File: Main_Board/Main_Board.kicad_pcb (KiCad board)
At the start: 4 copper layers, 35 parts, among them IC1 ZLDO1117K33TC, U1 STM32L152ZCTx

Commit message: Updated PCB
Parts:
- removed 56k (x2): R_2816_7142Metric_Pad3.20x4.45mm_HandSolder, Resistor_SMD:R_2816_7142Metric_Pad3.20x4.45mm_HandSolder
- removed 5Vin2: 5Vin, MountingHole:MountingHole_3mm_Pad
- removed CTimer (x2): CP_Elec_3x5.3, Capacitor_SMD:CP_Elec_3x5.3
- removed DIG0, DIG0_Matrix, DIG1, DIG1_Matrix, DIG2, DIG2_Matrix, DIG3, DIG3_Matrix, DIG4, DIG4_Matrix, DIG5, DIG5_Matrix, DIG6, DIG6_Matrix, DIG7, DIG7_Matrix: SolderWirePad_1x01_SMD_5x10mm, Connector_Wire:SolderWirePad_1x01_SMD_5x10mm
- removed GND: GND, MountingHole:MountingHole_3mm_Pad
- removed IC1: ZLDO1117K33TC, ZLDO1117K33TC-pcb-part-libraries:TO-252_1
- removed JTAGHeader1: Conn_ARM_JTAG_SWD_20, Connector_IDC:IDC-Header_2x06_P2.54mm_Horizontal
- removed Matrix_Cntrl1, TimerCntrl1: MAX6951CEE+, MAXIM:MAX6951CEE&plus_
- removed R4: R, Resistor_SMD:R_2816_7142Metric_Pad3.20x4.45mm_HandSolder
- removed REF** (x2): SolderWirePad_1x01_SMD_1x2mm, Connector_Wire:SolderWirePad_1x01_SMD_1x2mm
- removed Rx, Tx: MountingHole_Pad, MountingHole:MountingHole_3mm_Pad
- added 5V-3V3: ZLDO1117K33TC, TO-252_1, F.Cu at (166.2, 46.8)
- added 5V1: MountingHole_Pad, MountingHole:MountingHole_4.3mm_M4_Pad, F.Cu at (161.3, 30.5)
- added 7SEGDriver1: MAX6951CEE+, SOP64P602X173-17N, F.Cu at (111.3, 103.8)
- added BL1: MountingHole_Pad, MountingHole:MountingHole_4.3mm_M4_Pad_Via, F.Cu at (72.9, 116.7)
- added BR1: MountingHole_Pad, MountingHole:MountingHole_4.3mm_M4_Pad_Via, F.Cu at (191.7, 116.7)
- added C0: 100n, SamacSys_Parts:CAPC1005X55N, B.Cu at (111.8, 75.7)
- added C1: 100n, SamacSys_Parts:CAPC1005X55N, B.Cu at (115.8, 75.2)
- added C10: 100n, SamacSys_Parts:CAPC1005X55N, B.Cu at (111.8, 65.7)
- added C11: 100n, SamacSys_Parts:CAPC1005X55N, B.Cu at (111.7, 71.0)
- added C2: 100n, SamacSys_Parts:CAPC1005X55N, B.Cu at (121.5, 75.2)
- added C3: 100n, SamacSys_Parts:CAPC1005X55N, B.Cu at (128.0, 75.7)
- added C4: 100n, SamacSys_Parts:CAPC1005X55N, B.Cu at (127.1, 70.6)
- added C5: 100n, SamacSys_Parts:CAPC1005X55N, B.Cu at (127.0, 65.4)
- added C6: 100n, SamacSys_Parts:CAPC1005X55N, B.Cu at (127.5, 59.0)
- added C7: 100n, SamacSys_Parts:CAPC1005X55N, B.Cu at (120.5, 59.5)
- added C8: 100n, SamacSys_Parts:CAPC1005X55N, B.Cu at (115.2, 59.7)
- added C9: 100n, SamacSys_Parts:CAPC1005X55N, B.Cu at (111.6, 59.8)
- added CA0: 1u, SamacSys_Parts:CAPC1005X55N, B.Cu at (114.6, 62.5)
- added CA1: 10n, SamacSys_Parts:CAPC1005X55N, B.Cu at (114.6, 64.1)
- added CSET7SEG1: C_Small, Capacitor_SMD:C_1812_4532Metric_Pad1.57x3.40mm_HandSolder, F.Cu at (111.5, 109.1)
- added CSETLED1: C_Small, Capacitor_SMD:C_1812_4532Metric_Pad1.57x3.40mm_HandSolder, F.Cu at (81.5, 67.8)
- added Cbulk1: 4u7, SamacSys_Parts:CAPPRD200W52D500H1250, F.Cu at (176.0, 49.3)
- added Crst0: C, Capacitor_SMD:C_1812_4532Metric_Pad1.57x3.40mm_HandSolder, F.Cu at (175.8, 86.2)
- added GND1: MountingHole_Pad, MountingHole:MountingHole_4.3mm_M4_Pad, F.Cu at (172.2, 30.5)
- added HALLOUT1: MountingHole_Pad, MountingHole:MountingHole_2.7mm_Pad, F.Cu at (98.2, 29.2)
- added HALLSEL[0]1: MountingHole_Pad, MountingHole:MountingHole_2.7mm_Pad, F.Cu at (120.7, 29.2)
- added HALLSEL[1]1: MountingHole_Pad, MountingHole:MountingHole_2.7mm_Pad, F.Cu at (113.2, 29.2)
- added HALLSEL[2]1: MountingHole_Pad, MountingHole:MountingHole_2.7mm_Pad, F.Cu at (105.7, 29.2)
- added JTAGHEADER1: Conn_02x05_Odd_Even, Connector_PinHeader_2.00mm:PinHeader_2x05_P2.00mm_Vertical, F.Cu at (194.9, 64.1)
- added LA0: 39n, Inductor_SMD:L_01005_0402Metric_Pad0.57x0.30mm_HandSolder, B.Cu at (114.1, 66.0)
- added LEDDriver1: MAX6951CEE+, SOP64P602X173-17N, F.Cu at (87.9, 68.0)
- added R1: R_Small, Resistor_THT:R_Axial_DIN0309_L9.0mm_D3.2mm_P12.70mm_Horizontal, F.Cu at (152.7, 82.2)
- added R2: R, Resistor_THT:R_Axial_DIN0309_L9.0mm_D3.2mm_P12.70mm_Horizontal, F.Cu at (151.2, 39.9)
- added RSET7SEG1: R_Small, Resistor_THT:R_Axial_DIN0309_L9.0mm_D3.2mm_P12.70mm_Horizontal, F.Cu at (88.4, 105.9)
- added RSETLED1: R_Small, Resistor_THT:R_Axial_DIN0309_L9.0mm_D3.2mm_P12.70mm_Horizontal, F.Cu at (98.5, 67.6)
- added SEG0_7SEG1: MountingHole_Pad, MountingHole:MountingHole_2.5mm_Pad, F.Cu at (105.2, 117.9)
- added SEG0_LED1: MountingHole_Pad, MountingHole:MountingHole_2.5mm_Pad, F.Cu at (73.8, 64.6)
- added SEG1_7SEG1: MountingHole_Pad, MountingHole:MountingHole_2.5mm_Pad, F.Cu at (97.8, 117.9)
- added SEG1_LED1: MountingHole_Pad, MountingHole:MountingHole_2.5mm_Pad, F.Cu at (73.8, 56.9)
- added SEG2_7SEG1: MountingHole_Pad, MountingHole:MountingHole_2.5mm_Pad, F.Cu at (90.3, 117.9)
- added SEG2_LED1: MountingHole_Pad, MountingHole:MountingHole_2.5mm_Pad, F.Cu at (73.8, 49.2)
- added SEG3_7SEG1: MountingHole_Pad, MountingHole:MountingHole_2.5mm_Pad, F.Cu at (82.8, 117.9)
- added SEG3_LED1: MountingHole_Pad, MountingHole:MountingHole_2.5mm_Pad, F.Cu at (73.8, 41.4)
- added SEG4_7SEG1: MountingHole_Pad, MountingHole:MountingHole_2.5mm_Pad, F.Cu at (142.9, 117.9)
- added SEG4_LED1: MountingHole_Pad, MountingHole:MountingHole_2.5mm_Pad, F.Cu at (73.8, 103.3)
- added SEG5_7SEG1: MountingHole_Pad, MountingHole:MountingHole_2.5mm_Pad, F.Cu at (135.4, 117.9)
- added SEG5_LED1: MountingHole_Pad, MountingHole:MountingHole_2.5mm_Pad, F.Cu at (73.8, 95.5)
- added SEG6_7SEG1: MountingHole_Pad, MountingHole:MountingHole_2.5mm_Pad, F.Cu at (127.9, 117.9)
- added SEG6_LED1: MountingHole_Pad, MountingHole:MountingHole_2.5mm_Pad, F.Cu at (73.8, 87.8)
- added SEG7_7SEG1: MountingHole_Pad, MountingHole:MountingHole_2.5mm_Pad, F.Cu at (120.4, 117.9)
- added SEG7_LED1: MountingHole_Pad, MountingHole:MountingHole_2.5mm_Pad, F.Cu at (73.8, 80.1)
- added SEG8_7SEG1: MountingHole_Pad, MountingHole:MountingHole_2.5mm_Pad, F.Cu at (113.0, 117.9)
- added SEG8_LED1: MountingHole_Pad, MountingHole:MountingHole_2.5mm_Pad, F.Cu at (73.8, 72.4)
- added TL1: MountingHole_Pad, MountingHole:MountingHole_4.3mm_M4_Pad_Via, F.Cu at (73.1, 29.6)
- added TR1: MountingHole_Pad, MountingHole:MountingHole_4.3mm_M4_Pad_Via, F.Cu at (192.2, 29.5)
- added UART_Rx1: MountingHole_Pad, MountingHole:MountingHole_2.7mm_Pad, F.Cu at (161.9, 118.1)
- added UART_Tx1: MountingHole_Pad, MountingHole:MountingHole_2.7mm_Pad, F.Cu at (154.9, 118.1)
- added nRST1: SW_MEC_5G, Button_Switch_SMD:Panasonic_EVQPUL_EVQPUC, F.Cu at (157.6, 88.6)
- R3: footprint Resistor_SMD:R_2816_7142Metric_Pad3.20x4.45mm_HandSolder -> Resistor_THT:R_Axial_DIN0309_L9.0mm_D3.2mm_P12.70mm_Horizontal
- moved LED3V3 122.7 mm to (157.9, 47.2), turned to 0 degrees
- moved LED5V1 119.0 mm to (157.7, 40.6), turned to 0 degrees
- moved R3 116.5 mm to (144.5, 40.0), turned to 90 degrees
- moved U1 9.09 mm to (119.5, 67.4)
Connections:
- net /LED_Matrix_NSS renamed SPI3_NSS
- net /PH0OSC_IN renamed Net-(U1-Pad23)
- net /PH1OSC_OUT renamed Net-(U1-Pad24)
- net /PH2 renamed Net-(U1-Pad106)
- net /SPI1_MISO_AF5 renamed Net-(U1-Pad42)
- net /USART1_CK renamed Net-(U1-Pad100)
- net /USART1_CTS renamed Net-(U1-Pad103)
- net /USART1_RTS renamed Net-(U1-Pad104)
- net Net-(U1-Pad111) renamed SPI3_SCK
- net Net-(U1-Pad113) renamed SPI3_MOSI
- net Net-(U1-Pad134) renamed JTRST
- U1 pad 101: /USART1_TX_AF7 -> USART1_TX
- U1 pad 102: /USART1_RX_AF7 -> USART1_RX
- U1 pad 105: /JTMS-SWDIO -> JTMS-SWDIO
- U1 pad 107: +3V3 -> GND
- U1 pad 108: Net-(U1-Pad108) -> +3V3
- U1 pad 109: /JTCK-SWCLK -> JTCK-SWCLK
- U1 pad 110: /JTDI -> JTDI
- U1 pad 120: +3V3 -> GND
- U1 pad 121: Net-(U1-Pad121) -> +3V3
- U1 pad 130: +3V3 -> GND
- U1 pad 131: Net-(U1-Pad131) -> +3V3
- U1 pad 133: /JTDO -> JTDO-SWO
- U1 pad 143: +3V3 -> GND
- U1 pad 144: Net-(U1-Pad144) -> +3V3
- U1 pad 16: +3V3 -> GND
- U1 pad 17: Net-(U1-Pad17) -> +3V3
- U1 pad 25: Net-(U1-Pad25) -> +3V3
- U1 pad 30: Net-(U1-Pad30) -> GND
- U1 pad 33: Net-(U1-Pad33) -> +3.3VA
- U1 pad 34: /Hall_Select_[0] -> HALLSEL[0]
- U1 pad 35: /Hall_Select_[1] -> HALLSEL[1]
- U1 pad 36: /Hall_Select_[2] -> HALLSEL[2]
- U1 pad 37: /7Seg_NSS -> HALLOUT
- U1 pad 38: +3V3 -> GND
- U1 pad 39: Net-(U1-Pad39) -> +3V3
- U1 pad 41: /SPI1_SCK_AF5 -> DACOUT_2
- U1 pad 43: /SPI1_MOSI_AF5 -> SPI1_MOSI
- U1 pad 51: +3V3 -> GND
- U1 pad 52: Net-(U1-Pad52) -> +3V3
- U1 pad 61: +3V3 -> GND
- U1 pad 62: Net-(U1-Pad62) -> +3V3
- U1 pad 65: Net-(U1-Pad65) -> SPI1_NSS
- U1 pad 66: Net-(U1-Pad66) -> SPI1_SCK
- U1 pad 71: +3V3 -> GND
- U1 pad 72: Net-(U1-Pad72) -> +3V3
- U1 pad 73: Net-(U1-Pad73) -> SPI2_NSS
- U1 pad 74: Net-(U1-Pad74) -> SPI2_SCK
- U1 pad 76: Net-(U1-Pad76) -> SPI2_MOSI
- U1 pad 83: +3V3 -> GND
- U1 pad 84: Net-(U1-Pad84) -> +3V3
- U1 pad 94: +3V3 -> GND
- U1 pad 95: Net-(U1-Pad95) -> +3V3
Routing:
- net JTMS-SWDIO: track 0.00 -> 73.3 mm
- net JTDI: track 0.00 -> 71.8 mm, vias 0 -> 2
- net JTCK-SWCLK: track 0.00 -> 68.6 mm
- net JTDO-SWO: track 0.00 -> 64.4 mm
- net GND: track 58.0 -> 116.9 mm, vias 8 -> 30
- net USART1_RX: track 0.00 -> 58.0 mm
- net USART1_TX: track 0.00 -> 52.8 mm
- net /SEG4_LED: track 0.00 -> 41.3 mm
- net HALLOUT: track 0.00 -> 38.0 mm
- net /DIG_4_Matrix: track 36.8 -> 0.00 mm
- net /DIG_3_Matrix: track 36.4 -> 0.00 mm
- net /DIG_5_Matrix: track 35.9 -> 0.00 mm
- net /SEG4_7SEG: track 0.00 -> 35.1 mm
- net HALLSEL[0]: track 0.00 -> 32.7 mm
- net /SEG3_7SEG: track 0.00 -> 32.2 mm
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- added copper zone on In2.Cu, net +3V3
- added copper zone on In1.Cu, net GND
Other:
- net class 5V added: clearance 0.2, trace_width 1.27, via_dia 2.54, via_drill 1.524

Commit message: Updated Mainboard
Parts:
- removed 5V-3V3: ZLDO1117K33TC, TO-252_1
- removed C11: 100n, SamacSys_Parts:CAPC1005X55N
- removed Crst0: C, Capacitor_SMD:C_1812_4532Metric_Pad1.57x3.40mm_HandSolder
- removed HALLOUT1, HALLSEL[0]1, HALLSEL[1]1, HALLSEL[2]1, UART_Rx1, UART_Tx1: MountingHole_Pad, MountingHole:MountingHole_2.7mm_Pad
- removed R1: R_Small, Resistor_THT:R_Axial_DIN0309_L9.0mm_D3.2mm_P12.70mm_Horizontal
- removed SEG0_7SEG1, SEG0_LED1, SEG1_7SEG1, SEG1_LED1, SEG2_7SEG1, SEG2_LED1, SEG3_7SEG1, SEG3_LED1, SEG4_7SEG1, SEG4_LED1, SEG5_7SEG1, SEG5_LED1, SEG6_7SEG1, SEG6_LED1, SEG7_7SEG1, SEG7_LED1, SEG8_7SEG1, SEG8_LED1: MountingHole_Pad, MountingHole:MountingHole_2.5mm_Pad
- removed nRST1: SW_MEC_5G, Button_Switch_SMD:Panasonic_EVQPUL_EVQPUC
- added C12: 0.1u, SamacSys_Parts:CAPC2012X95N, F.Cu at (141.2, 43.5)
- added C13: 10u, SamacSys_Parts:CAPC2012X140N, F.Cu at (145.5, 40.3)
- added C14: 0.1u, SamacSys_Parts:CAPC2012X95N, F.Cu at (165.5, 45.2)
- added C15: 0.1u, SamacSys_Parts:CAPC2012X95N, F.Cu at (158.1, 47.5)
- added C16: 250u, Capacitor_THT:CP_Radial_D4.0mm_P2.00mm, F.Cu at (161.1, 38.5)
- added C18: 100n, SamacSys_Parts:CAPC2012X95N, F.Cu at (183.2, 46.5)
- added C19: 100n, SamacSys_Parts:CAPC2012X95N, F.Cu at (180.7, 46.6)
- added HallSensorHeader1: Conn_01x04_Male, Connector_PinHeader_2.54mm:PinHeader_1x04_P2.54mm_Vertical, F.Cu at (113.2, 26.6)
- added IC1: AZ1085CD-3.3TRG1, AZ1085CD33TRG1, F.Cu at (174.3, 49.6)
- added LED_Header1: Conn_01x09_Male, Connector_PinHeader_2.54mm:PinHeader_1x09_P2.54mm_Vertical, F.Cu at (70.6, 57.8)
- added LED_Header2: Conn_01x09_Male, Connector_PinHeader_2.54mm:PinHeader_1x09_P2.54mm_Vertical, F.Cu at (100.6, 119.4)
- added R4: 3300, Resistor_THT:R_Axial_DIN0309_L9.0mm_D3.2mm_P12.70mm_Horizontal, F.Cu at (126.9, 40.3)
- added R5: 150, Resistor_THT:R_Axial_DIN0309_L9.0mm_D3.2mm_P12.70mm_Horizontal, F.Cu at (126.8, 44.5)
- added R6: 100, Resistor_THT:R_Axial_DIN0309_L9.0mm_D3.2mm_P12.70mm_Horizontal, F.Cu at (142.1, 40.3)
- added R7: 10, Resistor_THT:R_Axial_DIN0309_L9.0mm_D3.2mm_P12.70mm_Horizontal, F.Cu at (158.0, 51.5)
- added SD_CARD1: 47352-1001, 47352-1001, F.Cu at (180.1, 73.5)
- added Speaker+1: MountingHole_Pad, MountingHole:MountingHole_2.5mm_Pad, F.Cu at (153.6, 28.4)
- added Speaker-1: MountingHole_Pad, MountingHole:MountingHole_2.5mm_Pad, F.Cu at (145.1, 28.2)
- added U2: LM386, SamacSys_Parts:SOP65P490X110-8N, F.Cu at (155.8, 43.8)
- added UARTHeader1: Conn_01x02_Male, Connector_PinHeader_2.54mm:PinHeader_1x02_P2.54mm_Vertical, F.Cu at (159.6, 119.5)
- C0, C1, C10, C2, C3, C4, C5, C6, C7, C8, C9: footprint SamacSys_Parts:CAPC1005X55N -> SamacSys_Parts:CAPC2012X95N
- CA0, LA0: moved to F.Cu
- CA1: footprint SamacSys_Parts:CAPC1005X55N -> SamacSys_Parts:CAPC2012X140N; moved to F.Cu
- CSET7SEG1, CSETLED1: value C_Small -> 47p; footprint Capacitor_SMD:C_1812_4532Metric_Pad1.57x3.40mm_HandSolder -> SamacSys_Parts:CAPC2012X75N
- RSET7SEG1, RSETLED1: value R_Small -> 47k; footprint Resistor_THT:R_Axial_DIN0309_L9.0mm_D3.2mm_P12.70mm_Horizontal -> SamacSys_Parts:RESC2012X60N
- moved LED5V1 109.2 mm to (237.3, 115.3), turned to 180 degrees
- moved R2 105.1 mm to (239.0, 97.8)
- moved R3 105.1 mm to (232.2, 97.9)
- moved LED3V3 100.3 mm to (237.1, 108.6), turned to 180 degrees
- moved JTAGHEADER1 31.8 mm to (194.3, 95.9)
- moved RSET7SEG1 20.1 mm to (108.4, 107.7), turned to 0 degrees
- moved RSETLED1 14.6 mm to (84.1, 65.1), turned to 270 degrees
- moved LA0 14.5 mm to (112.5, 51.5), turned to 180 degrees
- moved C8 11.9 mm to (111.7, 71.0), turned to 270 degrees
- moved CA1 11.4 mm to (113.2, 52.9)
- moved Cbulk1 11.1 mm to (186.6, 45.8)
- moved CA0 8.24 mm to (112.8, 54.5)
- moved 5V1 7.80 mm to (169.1, 30.5)
- moved GND1 7.66 mm to (179.8, 30.7), turned to 0 degrees
- moved CSETLED1 2.73 mm to (83.8, 69.2)
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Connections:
- U1 pad 112: Net-(U1-Pad112) -> SPI3_MISO
- U1 pad 114: Net-(U1-Pad114) -> SPI3_NSS
- U1 pad 25: +3V3 -> Net-(U1-Pad25)
- U1 pad 40: SPI3_NSS -> Net-(U1-Pad40)
- U1 pad 41: DACOUT_2 -> DAC_OUT
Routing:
- net GND: track 116.9 -> 179.7 mm, vias 30 -> 32
- net SPI3_MISO: track 0.00 -> 60.3 mm, vias 0 -> 2
- net SPI3_SCK: track 0.00 -> 60.0 mm, vias 0 -> 2
- net SPI3_MOSI: track 0.00 -> 57.8 mm, vias 0 -> 2
- net SPI3_NSS: track 0.00 -> 57.0 mm, vias 0 -> 2
- net +3V3: track 61.7 -> 97.6 mm, vias 27 -> 26
- net DAC_OUT: track 0.00 -> 28.0 mm, vias 0 -> 1
- net Net-(7SEGDriver1-Pad7): track 20.3 -> 3.26 mm, vias 1 -> 0
- net /SEG4_LED: track 41.3 -> 24.3 mm, vias 0 -> 1
- net +5V: track 14.9 -> 29.1 mm
- net Net-(LEDDriver1-Pad7): track 17.4 -> 3.45 mm, vias 1 -> 0
- net Net-(C16-Pad1): track 0.00 -> 13.5 mm
- net /SEG4_7SEG: track 35.1 -> 23.6 mm, vias 0 -> 1
- net Net-(C15-Pad1): track 0.00 -> 9.93 mm, vias 0 -> 1
- net Net-(C13-Pad1): track 0.00 -> 9.55 mm
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
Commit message: A
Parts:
- added C11: 30p, Capacitor_SMD:C_1206_3216Metric_Pad1.33x1.80mm_HandSolder, F.Cu at (121.9, 44.0)
- added C17: 22u, SamacSys_Parts:CAPC2012X95N, F.Cu at (104.1, 61.9)
- added C20: 22u, SamacSys_Parts:CAPC2012X95N, F.Cu at (111.1, 84.0)
- added C24: 30p, Capacitor_SMD:C_1206_3216Metric_Pad1.33x1.80mm_HandSolder, F.Cu at (113.9, 44.0)
- added R1: 1M, SamacSys_Parts:RESC5025X70N, F.Cu at (117.7, 53.9)
- added Y1: Crystal, Crystal:Crystal_HC18-U_Vertical, F.Cu at (120.3, 48.1)
- JTAGHEADER1: footprint Connector_PinHeader_2.00mm:PinHeader_2x05_P2.00mm_Vertical -> Connector_PinHeader_2.54mm:PinHeader_2x05_P2.54mm_Vertical
- R4: footprint Resistor_THT:R_Axial_DIN0309_L9.0mm_D3.2mm_P12.70mm_Horizontal -> SamacSys_Parts:CRGCQ2512F3K3
- R5: footprint Resistor_THT:R_Axial_DIN0309_L9.0mm_D3.2mm_P12.70mm_Horizontal -> SamacSys_Parts:ERJ1TRQF1R0U
- R6: footprint Resistor_THT:R_Axial_DIN0309_L9.0mm_D3.2mm_P12.70mm_Horizontal -> SamacSys_Parts:RESC5025X70N
- moved LED3V3 96.5 mm to (155.7, 57.0), turned to 90 degrees
- moved LED5V1 95.7 mm to (161.4, 57.0), turned to 90 degrees
- moved R2 82.9 mm to (163.7, 63.1), turned to 270 degrees
- moved C18 82.5 mm to (102.1, 61.9)
- moved R3 81.9 mm to (158.1, 63.1), turned to 270 degrees
- moved C19 79.8 mm to (111.2, 85.9), turned to 0 degrees
- moved JTAGHEADER1 67.0 mm to (127.6, 89.2), turned to 90 degrees
- moved C14 46.3 mm to (119.9, 37.2), turned to 270 degrees
- moved C16 46.1 mm to (115.5, 31.7)
- moved U2 40.7 mm to (115.6, 37.7)
- moved C15 40.1 mm to (118.6, 40.5), turned to 0 degrees
- moved UARTHeader1 38.4 mm to (127.5, 98.4)
- moved R6 38.1 mm to (104.0, 40.5), turned to 270 degrees
- moved SD_CARD1 37.0 mm to (154.3, 99.9), turned to 0 degrees
- moved BR1 36.4 mm to (161.9, 95.8)
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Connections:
- net JTRST renamed Net-(U1-Pad134)
- net Net-(U1-Pad138) renamed Boot
- U1 pad 23: Net-(U1-Pad23) -> /OSC_IN
- U1 pad 24: Net-(U1-Pad24) -> /OSC_OUT
- U1 pad 25: Net-(U1-Pad25) -> nRST
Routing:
- net JTMS-SWDIO: track 73.4 -> 9.74 mm
- net +3V3: track 97.6 -> 158.3 mm, vias 26 -> 36
- net JTCK-SWCLK: track 69.5 -> 10.5 mm
- net JTDI: track 68.0 -> 14.4 mm
- net +5V: track 29.1 -> 79.0 mm, vias 0 -> 2
- net JTDO-SWO: track 73.7 -> 24.1 mm
- net nRST: track 0.00 -> 46.5 mm, vias 0 -> 2
- net USART1_TX: track 55.9 -> 21.1 mm
- net USART1_RX: track 57.3 -> 23.3 mm
- net SPI3_SCK: track 60.0 -> 33.1 mm
- net SPI3_MISO: track 60.3 -> 36.1 mm, vias 2 -> 0
- net SPI3_MOSI: track 57.8 -> 35.8 mm, vias 2 -> 0
- net SPI3_NSS: track 57.0 -> 37.4 mm, vias 2 -> 0
- net GND: track 179.7 -> 161.2 mm, vias 32 -> 36
- net DAC_OUT: track 28.0 -> 11.3 mm, vias 1 -> 0
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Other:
- board text added: "Pawn Takes Pawn Mainboard PCB Aedan Frazier Bilal Sahla Max Baer Thomas Munsell"
- board text added: "Reset and Boot Hardware"

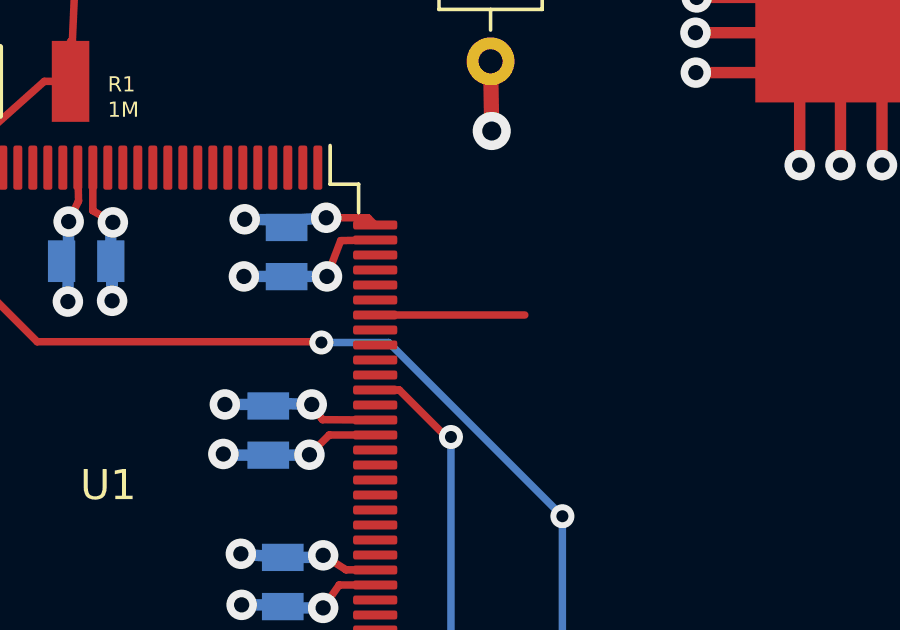
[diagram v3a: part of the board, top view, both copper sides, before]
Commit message: Added switch board, reset circuit
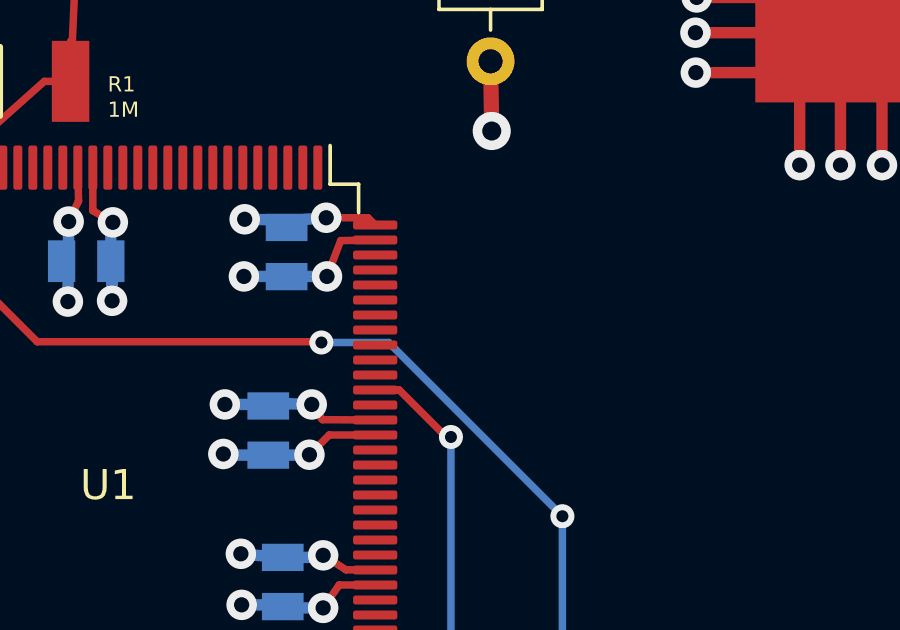
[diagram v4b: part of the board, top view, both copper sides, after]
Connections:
- U1 pad 138: Boot -> GND
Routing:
- net Boot: track 4.99 -> 0.00 mm
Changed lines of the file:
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@@
-(kicad_pcb (version 20171130) (host pcbnew "(5.1.10)-1")
+(kicad_pcb (version 20171130) (host pcbnew "(5.1.5)-3")
   (general
     (thickness 1.6)
     (drawings 11)
-    (tracks 628)
+    (tracks 627)
     (zones 0)
     (modules 59)
-    (nets 159)
+    (nets 158)
   )
   (page A4)
@@
     (2 In2.Cu signal hide)
     (31 B.Cu signal)
-    (32 B.Adhes user)
-    (33 F.Adhes user)
+    (32 B.Adhes user hide)
+    (33 F.Adhes user hide)
     (34 B.Paste user hide)
     (35 F.Paste user hide)
@@
   )
   (setup
-    (last_trace_width 0.508)
+    (last_trace_width 0.25)
     (user_trace_width 0.381)
     (user_trace_width 0.508)
@@
   (net 156 /OSC_IN)
   (net 157 /OSC_OUT)
-  (net 158 Boot)
   (net_class Default "This is the default net class."
     (clearance 0.2)
@@
     (add_net /SEG8_7SEG)
     (add_net /SEG8_LED)
-    (add_net Boot)
     (add_net DAC_OUT)
     (add_net GND)
@@
       (net 21 "Net-(U1-Pad139)"))
     (pad 138 smd roundrect (at -5.75 -10.6625 270) (size 0.3 1.475) (layers F.Cu F.Paste F.Mask) (roundrect_rratio 0.25)
-      (net 158 Boot))
+      (net 3 GND))
     (pad 137 smd roundrect (at -5.25 -10.6625 270) (size 0.3 1.475) (layers F.Cu F.Paste F.Mask) (roundrect_rratio 0.25)
       (net 22 "Net-(U1-Pad137)"))
@@
   (segment (start 115.48658 44.01058) (end 115.31386 44.0055) (width 0.25) (layer F.Cu) (net 157))
   (segment (start 115.38932 48.14824) (end 115.48658 44.01058) (width 0.25) (layer F.Cu) (net 157))
-  (segment (start 130.1695 61.687) (end 135.1565 61.687) (width 0.25) (layer F.Cu) (net 158))
   (zone (net 3) (net_name GND) (layer In1.Cu) (hatch edge 0.508)
     (connect_pads (clearance 0.508))

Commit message: 8 Hall Sensor
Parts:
- removed HallSensorHeader1: Conn_01x04_Male, Connector_PinHeader_2.54mm:PinHeader_1x04_P2.54mm_Vertical
- added C25: C_Small, SamacSys_Parts:CAPC2012X140N, F.Cu at (154.1, 68.4)
- added J1: Conn_01x08, Connector_PinHeader_2.54mm:PinHeader_1x08_P2.54mm_Vertical, F.Cu at (88.1, 71.4)
- added J2: Conn_01x03_Male, Connector_PinHeader_2.54mm:PinHeader_1x03_P2.54mm_Vertical, F.Cu at (113.2, 26.7)
- added R8: R_Small, SamacSys_Parts:RESC5025X70N, F.Cu at (138.8, 69.9)
- added e1: SW_MEC_5G, Button_Switch_SMD:SW_SPST_Omron_B3FS-105xP, F.Cu at (146.8, 69.8)
- moved LED_Header1 2.76 mm to (88.1, 47.1)
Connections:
- U1 pad 138: GND -> Boot
- U1 pad 37: HALLOUT -> Net-(U1-Pad37)
- U1 pad 53: Net-(U1-Pad53) -> HALLOUT[0]
- U1 pad 54: Net-(U1-Pad54) -> HALLOUT[1]
- U1 pad 55: Net-(U1-Pad55) -> HALLOUT[2]
- U1 pad 56: Net-(U1-Pad56) -> HALLOUT[3]
- U1 pad 57: Net-(U1-Pad57) -> HALLOUT[4]
- U1 pad 58: Net-(U1-Pad58) -> HALLOUT[5]
- U1 pad 59: Net-(U1-Pad59) -> HALLOUT[6]
- U1 pad 60: Net-(U1-Pad60) -> HALLOUT[7]
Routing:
- net HALLOUT: track 33.2 -> 0.00 mm, vias 1 -> 0
- net HALLOUT[7]: track 0.00 -> 28.6 mm, vias 0 -> 1
- net HALLOUT[6]: track 0.00 -> 27.5 mm, vias 0 -> 1
- net HALLOUT[5]: track 0.00 -> 26.5 mm, vias 0 -> 1
- net HALLOUT[4]: track 0.00 -> 25.6 mm, vias 0 -> 1
- net HALLOUT[3]: track 0.00 -> 25.0 mm, vias 0 -> 1
- net HALLOUT[2]: track 0.00 -> 24.2 mm, vias 0 -> 1
- net HALLOUT[1]: track 0.00 -> 23.3 mm, vias 0 -> 1
- net HALLOUT[0]: track 0.00 -> 22.7 mm, vias 0 -> 1
- net nRST: track 46.5 -> 64.6 mm
- net GND: track 161.2 -> 171.0 mm, vias 36 -> 38
- net Net-(U1-Pad48): track 8.24 -> 0.84 mm, vias 1 -> 0
- net Net-(U1-Pad47): track 6.92 -> 0.00 mm, vias 1 -> 0
- net Net-(U1-Pad46): track 6.88 -> 0.00 mm, vias 1 -> 0
- net Net-(U1-Pad45): track 6.62 -> 0.00 mm, vias 1 -> 0
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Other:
- board text removed: "Reset and Boot Hardware"
